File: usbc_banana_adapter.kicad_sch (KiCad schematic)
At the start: 10 parts, among them J1 USB_C_Receptacle, SW1 SW_DIP_x02, U1 TPS25810RVC

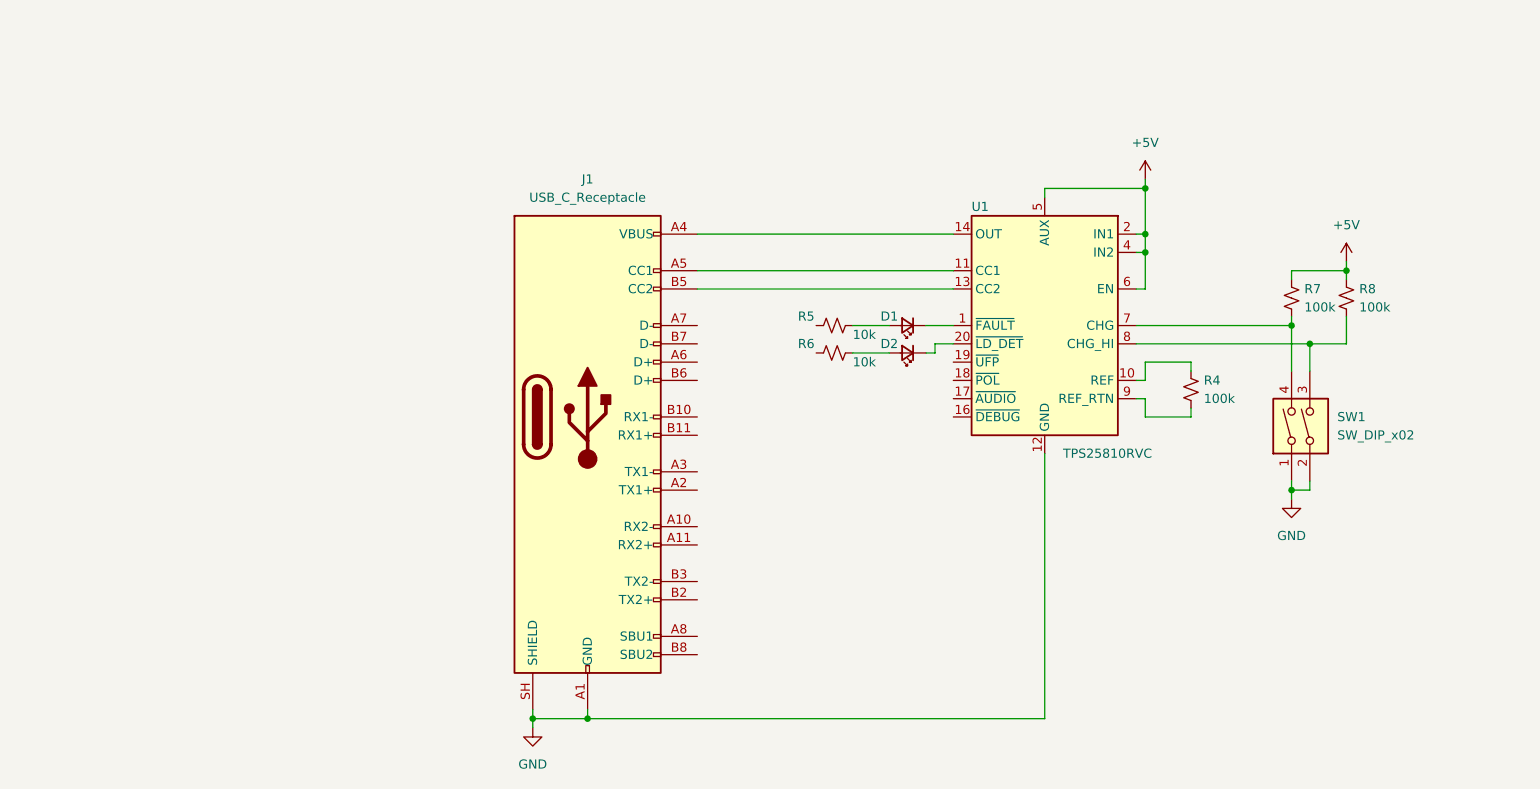
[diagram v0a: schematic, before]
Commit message: active proto negotiation
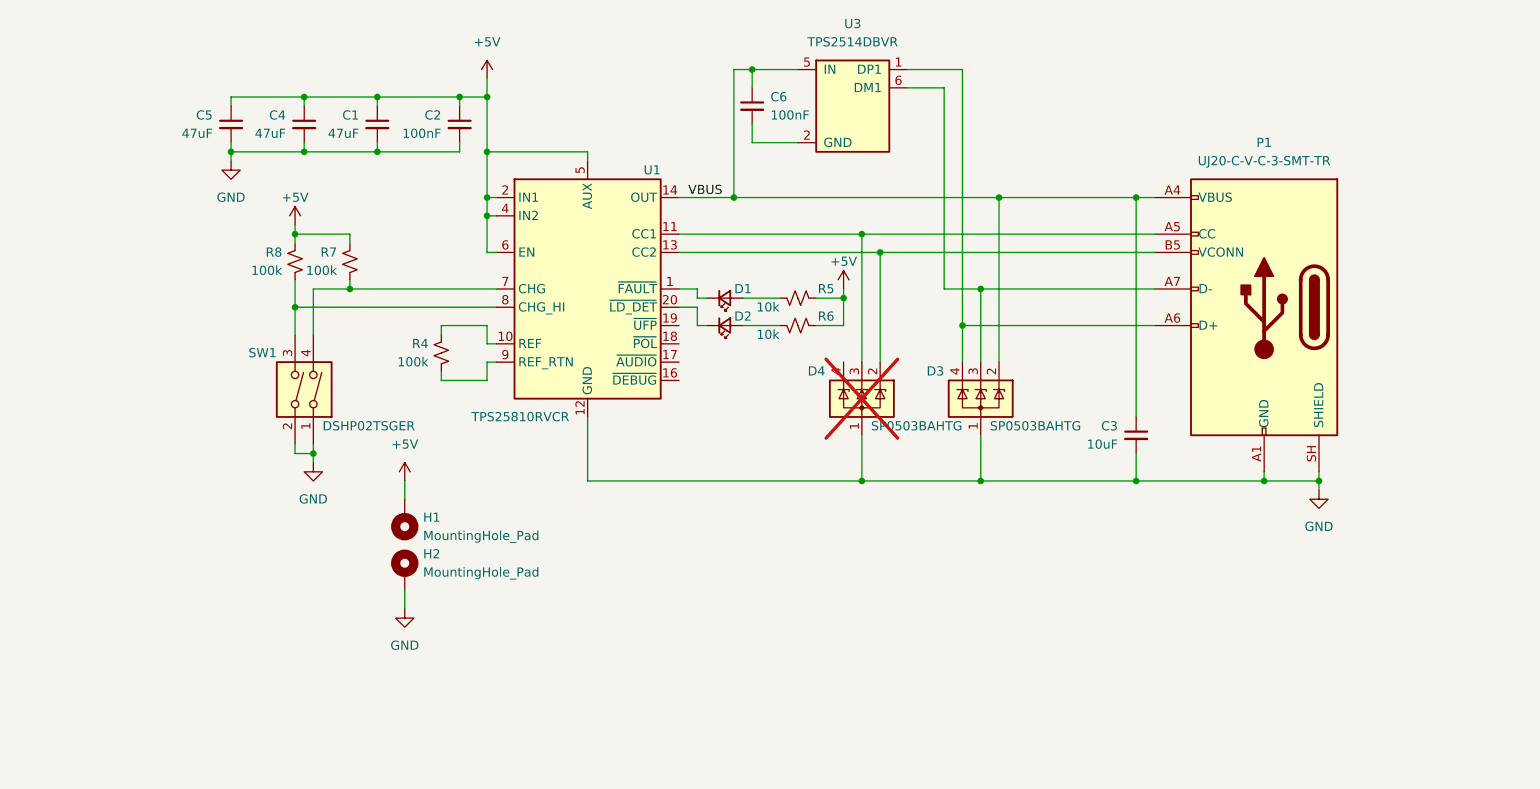
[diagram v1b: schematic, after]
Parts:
- removed J1: USB_C_Receptacle, symbol Connector:USB_C_Receptacle
- added C1, C4, C5: 47uF, Capacitor_SMD:C_1210_3225Metric_Pad1.33x2.70mm_HandSolder, symbol Device:C_Small
- added C2, C6: 100nF, Capacitor_SMD:C_0603_1608Metric_Pad1.08x0.95mm_HandSolder, symbol Device:C_Small
- added C3: 10uF, Capacitor_SMD:C_0805_2012Metric_Pad1.18x1.45mm_HandSolder, symbol Device:C_Small
- added D3, D4: SP0503BAHTG, Package_TO_SOT_SMD:SOT-143, symbol Power_Protection:SP0503BAHT
- added H1, H2: MountingHole_Pad, JSfootprints:MountingHole_4mmx10mm_#6_loose, symbol Mechanical:MountingHole_Pad
- added P1: UJ20-C-V-C-3-SMT-TR, JSfootprints:UJ20-C-V-C-3-SMT-TR, symbol Connector:USB_C_Plug_USB2.0
- added U3: TPS2514DBVR, Package_TO_SOT_SMD:SOT-23-6, symbol Interface_USB:TPS2514
- D1, D2: footprint (none) -> LED_SMD:LED_0603_1608Metric_Pad1.05x0.95mm_HandSolder
- SW1: value SW_DIP_x02 -> DSHP02TSGER; footprint (none) -> Button_Switch_SMD:SW_DIP_SPSTx02_Slide_KingTek_DSHP02TS_W7.62mm_P1.27mm
- U1: value TPS25810RVC -> TPS25810RVCR; LCSC PN (none) -> C473913
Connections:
- net +5V: now also R5.1, R6.1, C1.1, C2.1, C4.1, C5.1, H1.1
- net GND: now also C1.2, C2.2, C3.2, C4.2, C5.2, D3.1 (A), D4.1 (A), H2.1, P1.A1 (GND), P1.A12 (GND), P1.B1 (GND), P1.B12 (GND), P1.SH (SHIELD)
- net at U1.11 (CC1): now also D4.3 (K), P1.A5 (CC)
- net at U1.13 (CC2): now also D4.2 (K), P1.B5 (VCONN)
- net VBUS: now reaches U1.14 (OUT), U1.15 (OUT)
- net VBUS: now also C3.1, C6.1, D3.2 (K), P1.A4 (VBUS), P1.A9 (VBUS), P1.B4 (VBUS), P1.B9 (VBUS), U3.5 (IN)
- new net: D3.4 (K), P1.A6 (D+), U3.1 (DP1)
- new net: D3.3 (K), P1.A7 (D-), U3.6 (DM1)
- new net: C6.2, U3.2 (GND)
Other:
- moved on the sheet: D1, D2, R4, R5, R6, R7, R8, SW1, U1

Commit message: layout
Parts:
- added FID1, FID2, FID3: Fiducial, Fiducial:Fiducial_1mm_Mask2mm, symbol Mechanical:Fiducial
- added H3, H4: 6072, symbol Auxiliary_Items:MountingScrew
- added H5, H6: MountingHole, MountingHole:ToolingHole_1.152mm, symbol Mechanical:MountingHole
- added H7, H8: 96659A102, symbol Auxiliary_Items:MountingScrew
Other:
- note added: "Sub TPS2514ADBVR for apple"
- moved on the sheet: H1, H2

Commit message: layout
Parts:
- removed D2: LED_Small, LED_SMD:LED_0603_1608Metric_Pad1.05x0.95mm_HandSolder, symbol Device:LED_Small
- removed R6: 10k, Resistor_SMD:R_0603_1608Metric_Pad0.98x0.95mm_HandSolder, symbol Device:R_Small_US
- added R9: 0, Resistor_SMD:R_0603_1608Metric_Pad0.98x0.95mm_HandSolder, symbol Device:R_Small_US
- D4: now fitted; now in the parts list
- P1: symbol Connector:USB_C_Plug_USB2.0 -> Connector:USB_C_Receptacle_USB2.0_16P
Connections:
- net GND: now also C6.2, U3.2 (GND)
- net VBUS: now also D4.2 (K); no longer D3.2 (K)
- net at P1.A6 (D+), U3.1 (DP1): now also D3.3 (K), P1.B6 (D+), R9.2; no longer D3.4 (K)
- net at P1.A7 (D-), U3.6 (DM1): now also D3.4 (K), P1.B7 (D-), R9.1; no longer D3.3 (K)
- net at P1.B5 (CC2), U1.13 (CC2): now also D4.4 (K); no longer D4.2 (K)

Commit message: revA ready
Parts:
- added C7: 47uF, Capacitor_SMD:C_1206_3216Metric_Pad1.33x1.80mm_HandSolder, symbol Device:C_Small
- C1, C4, C5: footprint Capacitor_SMD:C_1210_3225Metric_Pad1.33x2.70mm_HandSolder -> Capacitor_SMD:C_1206_3216Metric_Pad1.33x1.80mm_HandSolder; LCSC PN (none) -> C96123; MPN (none) -> CL31A476MPHNNNE
- C2, C6: LCSC PN (none) -> C14663; MPN (none) -> CC0603KRX7R9BB104
- C3: LCSC PN (none) -> C440198; MPN (none) -> GRM21BR61H106KE43L
- D1: value LED_Small -> KT-0603R; LCSC PN (none) -> C2286; MPN (none) -> KT-0603R
- D3, D4: now not fitted
- P1: MPN (none) -> UJ20-C-V-C-3-SMT-TR
- R4, R7, R8: LCSC PN (none) -> C25803; MPN (none) -> 0603WAF1003T5E
- R5: LCSC PN (none) -> C25804; MPN (none) -> 0603WAF1002T5E
- R9: LCSC PN (none) -> C21189; MPN (none) -> 0603WAF0000T5E; now in the parts list
- SW1: value DSHP02TSGER -> DSHP02TJGER; footprint Button_Switch_SMD:SW_DIP_SPSTx02_Slide_KingTek_DSHP02TS_W7.62mm_P1.27mm -> Button_Switch_SMD:SW_DIP_SPSTx02_Slide_KingTek_DSHP02TJ_W5.25mm_P1.27mm_JPin; LCSC PN (none) -> C5301819; MPN (none) -> DSHP02TJGER
- U1: MPN (none) -> TPS25810RVCR
- U3: MPN (none) -> TPS2514DBVR
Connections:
- net +5V: now also SW1.1, SW1.2, C7.1; no longer R7.1, R8.1
- net GND: now also R7.2, R8.2, C7.2; no longer SW1.1, SW1.2
- net at SW1.4, U1.7 (CHG): now also R8.1; no longer R7.2
- net at SW1.3, U1.8 (CHG_HI): now also R7.1; no longer R8.2
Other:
- moved on the sheet: R7, R8, SW1

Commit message: swap banana
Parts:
- H3, H4: value 6072 -> 659; MPN (none) -> 659
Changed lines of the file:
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@@
 			)
 		)
-		(property "Value" "6072"
+		(property "Value" "659"
 			(at 81.28 114.046 0)
 			(show_name no)
@@
 			)
 		)
+		(property "MPN" "659"
+			(at 81.28 110.49 0)
+			(hide yes)
+			(show_name no)
+			(do_not_autoplace no)
+			(effects
+				(font
+					(size 1.27 1.27)
+				)
+			)
+		)
 		(instances
 			(project "usbc_banana_adapter"
@@
 			)
 		)
-		(property "Value" "6072"
+		(property "Value" "659"
 			(at 69.85 114.046 0)
 			(show_name no)
@@
 			(at 69.85 110.49 0)
 			(hide yes)
+			(show_name no)
+			(do_not_autoplace no)
+			(effects
+				(font
+					(size 1.27 1.27)
+				)
+			)
+		)
+		(property "MPN" "659"
+			(at 69.85 110.49 0)
+			(hide yes)

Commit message: add diode
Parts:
- added D2: SS54, Diode_SMD:D_SMA, symbol Device:D_Schottky_Small
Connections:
- net +5V: now also D2.1 (K)
- net GND: now also D2.2 (A)
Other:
- moved on the sheet: FID1, FID2, FID3, H3, H4, H5, H6, H7, H8
